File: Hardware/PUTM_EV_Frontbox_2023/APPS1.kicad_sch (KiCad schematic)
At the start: 23 parts, among them U22 MCP6N11-005, U23 MCP6001

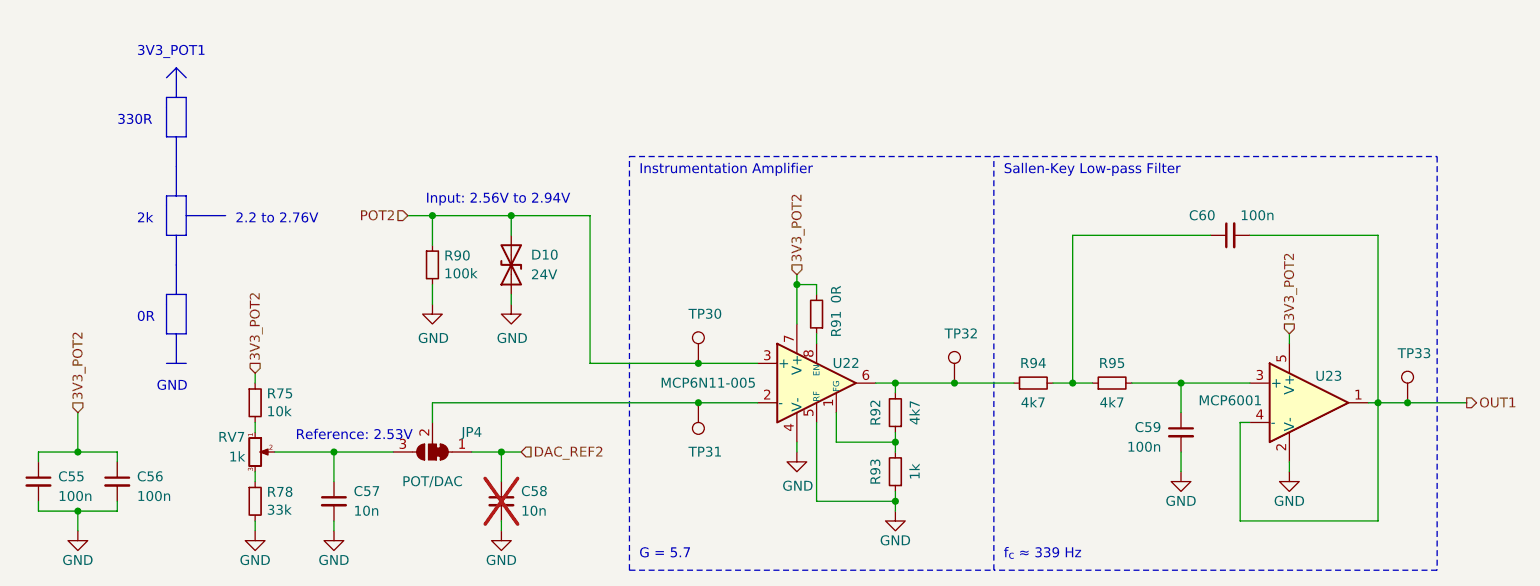
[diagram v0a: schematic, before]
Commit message: Changed board outline and layout to match ASB
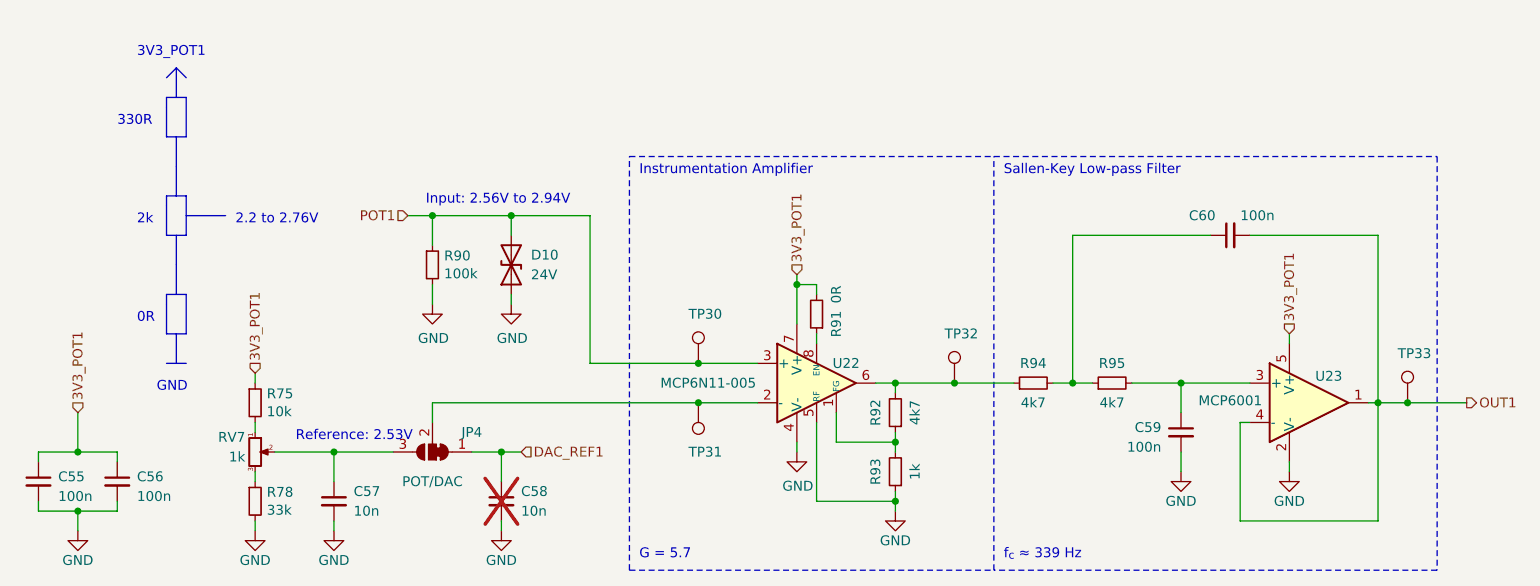
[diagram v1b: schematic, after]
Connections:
- net 3V3_POT2 renamed 3V3_POT1
- net DAC_REF2 renamed DAC_REF1
- net POT2 renamed POT1
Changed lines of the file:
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@@
     (effects (font (size 1.27 1.27)) (justify left bottom))
   )
-  (hierarchical_label "3V3_POT2" (shape input) (at 83.82 98.425 90) (fields_autoplaced)
+  (hierarchical_label "3V3_POT1" (shape input) (at 83.82 98.425 90) (fields_autoplaced)
     (effects (font (size 1.27 1.27)) (justify left))
   )
-  (hierarchical_label "3V3_POT2" (shape input) (at 217.17 93.345 90) (fields_autoplaced)
+  (hierarchical_label "3V3_POT1" (shape input) (at 217.17 93.345 90) (fields_autoplaced)
     (effects (font (size 1.27 1.27)) (justify left))
   )
-  (hierarchical_label "3V3_POT2" (shape input) (at 153.67 85.725 90) (fields_autoplaced)
+  (hierarchical_label "3V3_POT1" (shape input) (at 153.67 85.725 90) (fields_autoplaced)
     (effects (font (size 1.27 1.27)) (justify left))
   )
@@
     (effects (font (size 1.27 1.27)) (justify left))
   )
-  (hierarchical_label "3V3_POT2" (shape input) (at 60.96 103.505 90) (fields_autoplaced)
+  (hierarchical_label "3V3_POT1" (shape input) (at 60.96 103.505 90) (fields_autoplaced)
     (effects (font (size 1.27 1.27)) (justify left))
   )
-  (hierarchical_label "POT2" (shape input) (at 103.505 78.105 180) (fields_autoplaced)
+  (hierarchical_label "POT1" (shape input) (at 103.505 78.105 180) (fields_autoplaced)
     (effects (font (size 1.27 1.27)) (justify right))
   )
-  (hierarchical_label "DAC_REF2" (shape input) (at 118.11 108.585 0) (fields_autoplaced)
+  (hierarchical_label "DAC_REF1" (shape input) (at 118.11 108.585 0) (fields_autoplaced)
     (effects (font (size 1.27 1.27)) (justify left))
   )

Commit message: Removed APPS pots
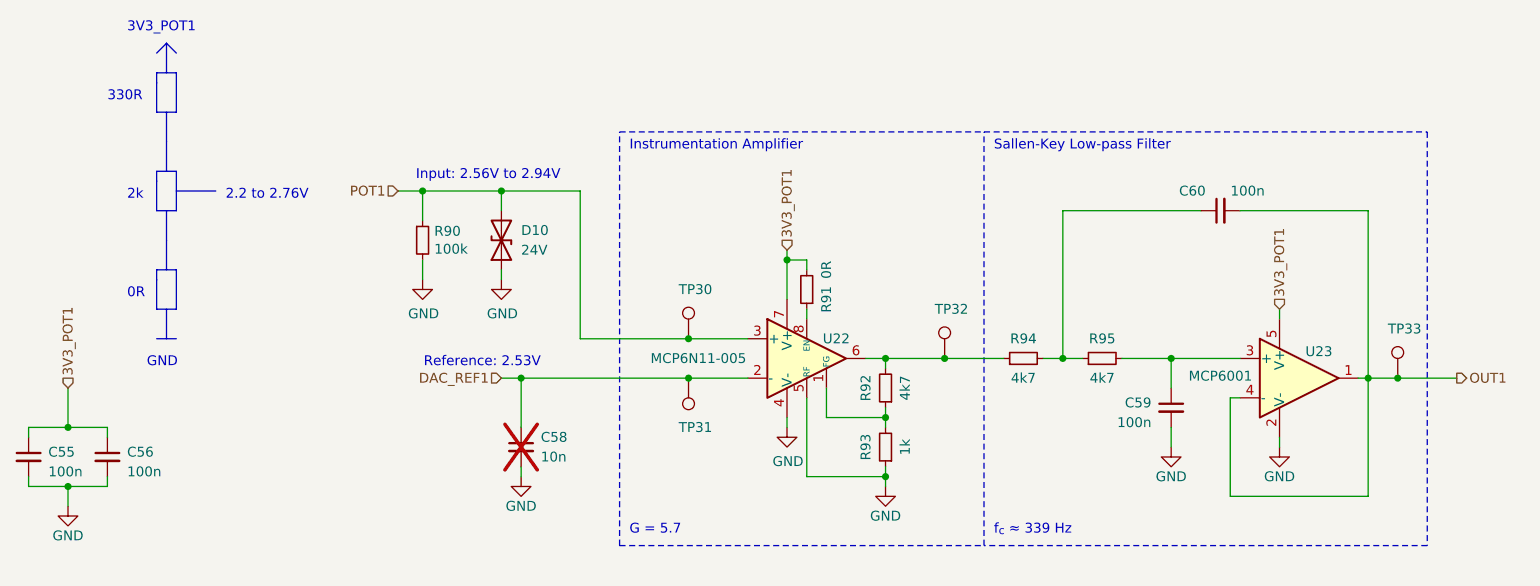
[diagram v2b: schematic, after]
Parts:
- removed C57: 10n, Capacitor_SMD:C_0603_1608Metric_Pad1.08x0.95mm_HandSolder, symbol Device:C_Small
- removed JP4: POT/DAC, Jumper:SolderJumper-3_P1.3mm_Bridged12_RoundedPad1.0x1.5mm, symbol Jumper:SolderJumper_3_Bridged12
- removed R75: 10k, Resistor_SMD:R_0603_1608Metric_Pad0.98x0.95mm_HandSolder, symbol Device:R_Small
- removed R78: 33k, Resistor_SMD:R_0603_1608Metric_Pad0.98x0.95mm_HandSolder, symbol Device:R_Small
- removed RV7: 1k, Potentiometer_SMD:Potentiometer_Bourns_3214J_Horizontal, symbol Device:R_Potentiometer_Small
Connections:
- net DAC_REF1: now also TP31.1, U22.2 (-)
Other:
- moved on the sheet: C55, C56, C58, C59, C60, D10, R90, R91, R92, R93, R94, R95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

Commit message: Routing
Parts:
- renumbered C55 to C49, C56 to C50, C58 to C52, C59 to C53, C60 to C54, D10 to D9, R90 to R69, R91 to R70, R92 to R71, R93 to R72, R94 to R73, R95 to R74, TP30 to TP26, TP31 to TP27, TP32 to TP28, TP33 to TP29, U22 to U18, U23 to U21
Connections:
- net 3V3_POT1 renamed 3V3_POT
- net DAC_REF1 renamed DAC_REF
- net OUT1 renamed OUT
- net POT1 renamed POT

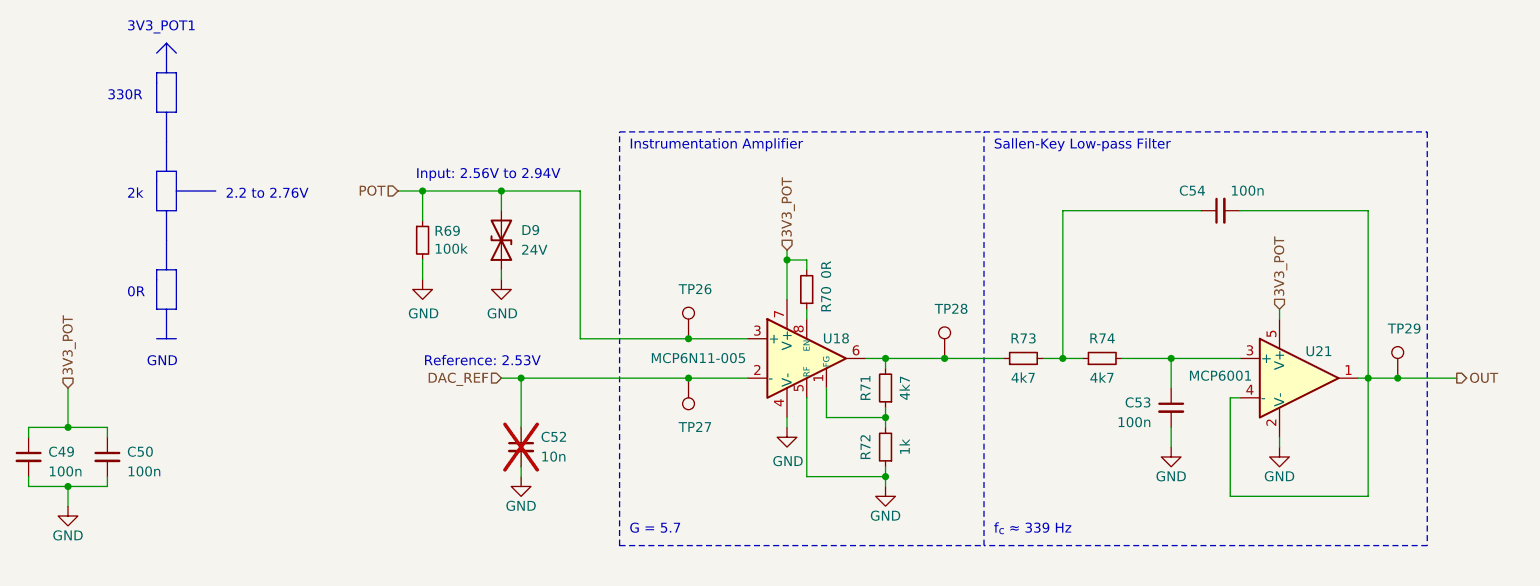
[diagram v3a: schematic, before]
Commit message: Added gearbox temperature sensors on schematic
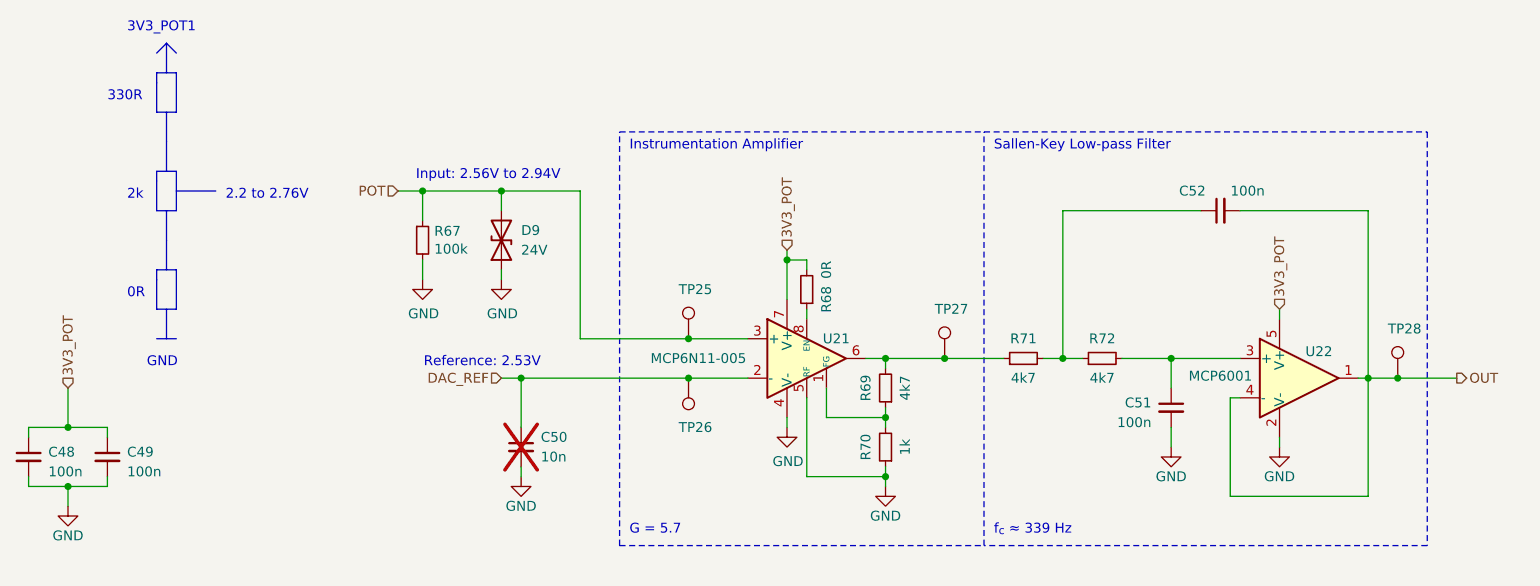
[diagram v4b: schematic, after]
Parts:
- renumbered C49 to C48, C50 to C49, C52 to C50, C53 to C51, C54 to C52, R69 to R67, R70 to R68, R71 to R69, R72 to R70, R73 to R71, R74 to R72, TP26 to TP25, TP27 to TP26, TP28 to TP27, TP29 to TP28, U18 to U21, U21 to U22
